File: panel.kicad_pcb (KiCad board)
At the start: 2 copper layers, 25.4 x 52.3 mm, 64 parts, among them U1 DF52-4S-0.8H(21), U2 DF52-4S-0.8H(21), U3 DF52-4S-0.8H(21)

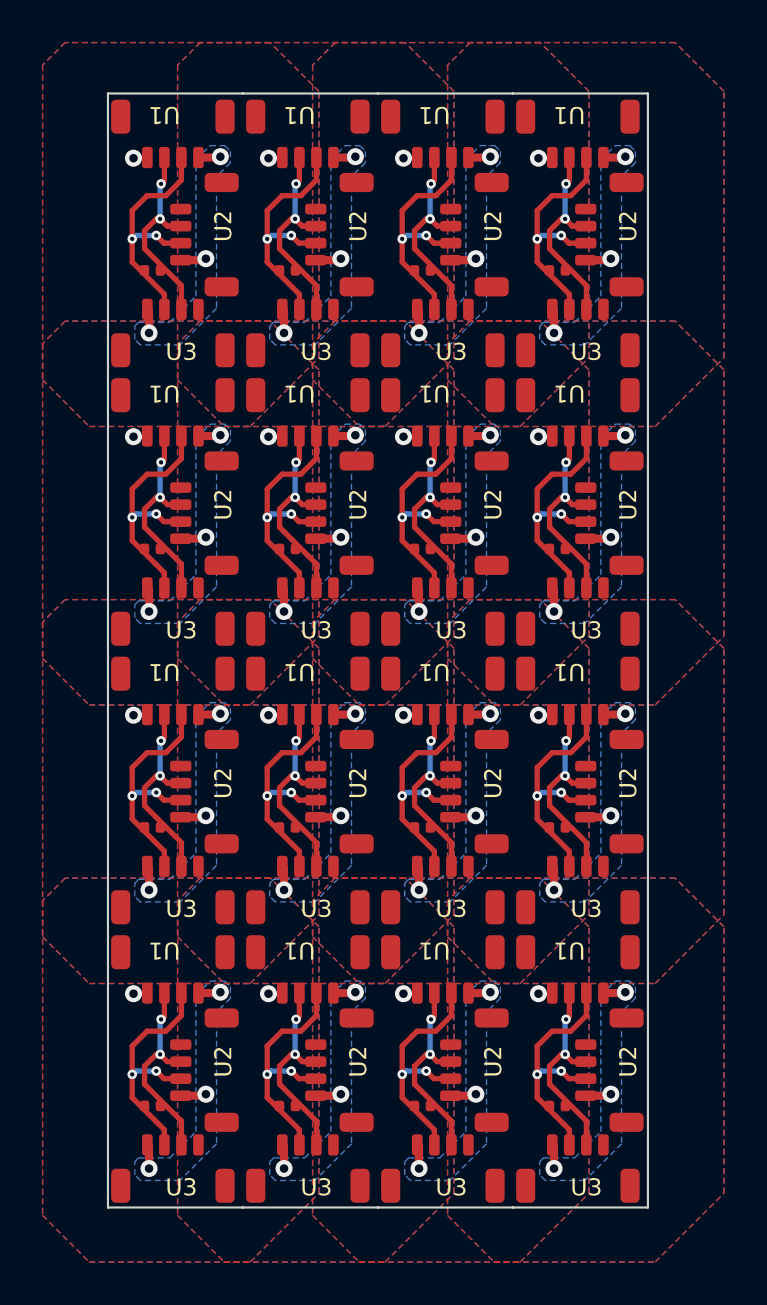
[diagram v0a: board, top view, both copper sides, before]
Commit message: updated gnd for panel. updated panel. updated panel script for better more better
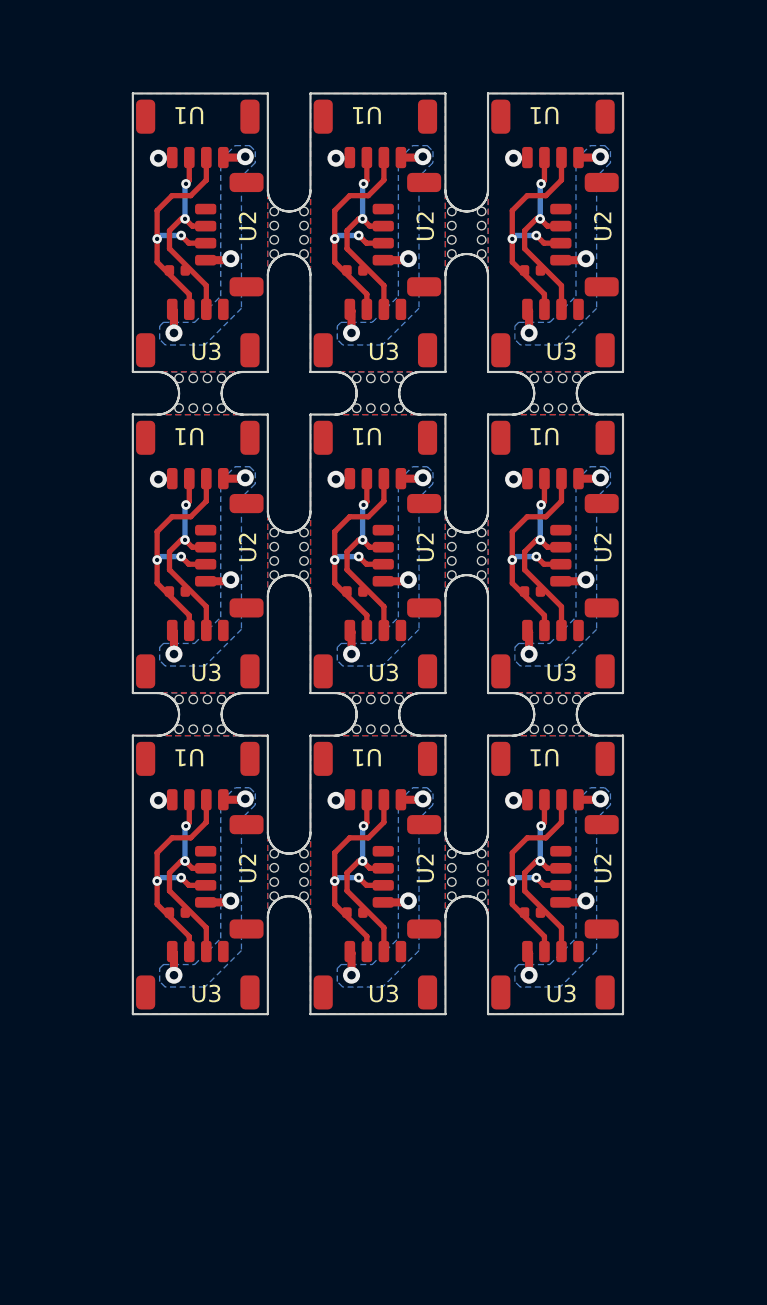
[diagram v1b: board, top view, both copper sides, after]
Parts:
- removed the R1 at (156.9, 67.5)
- removed the R1 at (150.6, 28.3)
- removed the R1 at (137.9, 28.3)
- removed the R1 at (156.9, 41.4)
- removed the R1 at (137.9, 41.4)
- removed the R1 at (137.9, 54.5)
- removed the R1 at (156.9, 28.3)
- removed the R1 at (144.2, 54.5)
- removed the R1 at (150.6, 41.4)
- removed the R1 at (156.9, 54.5)
- removed the R1 at (150.6, 54.5)
- removed the R1 at (144.2, 41.4)
- removed the R1 at (150.6, 67.5)
- removed the R1 at (144.2, 67.5)
- removed the R1 at (137.9, 67.5)
- removed the R1 at (144.2, 28.3)
- removed the U1 at (145.2, 62.2)
- removed the U1 at (157.9, 36.1)
- removed the U1 at (145.2, 49.2)
- removed the U1 at (145.2, 23.0)
- removed the U1 at (138.9, 49.2)
- removed the U1 at (151.6, 62.2)
- removed the U1 at (151.6, 49.2)
- removed the U1 at (157.9, 62.2)
- removed the U1 at (157.9, 23.0)
- removed the U1 at (138.9, 23.0)
- removed the U1 at (151.6, 23.0)
- removed the U1 at (138.9, 36.1)
- removed the U1 at (138.9, 62.2)
- removed the U1 at (157.9, 49.2)
- removed the U1 at (151.6, 36.1)
- removed the U1 at (145.2, 36.1)
- removed the U2 at (158.3, 52.8)
- removed the U2 at (145.6, 65.9)
- removed the U2 at (139.2, 26.6)
- removed the U2 at (145.6, 39.7)
- removed the U2 at (151.9, 39.7)
- removed the U2 at (139.2, 65.9)
- removed the U2 at (151.9, 52.8)
- removed the U2 at (158.3, 65.9)
- removed the U2 at (139.2, 39.7)
- removed the U2 at (151.9, 26.6)
- removed the U2 at (145.6, 26.6)
- removed the U2 at (158.3, 39.7)
- removed the U2 at (145.6, 52.8)
- removed the U2 at (139.2, 52.8)
- removed the U2 at (151.9, 65.9)
- removed the U2 at (158.3, 26.6)
- removed the U3 at (151.6, 56.3)
- removed the U3 at (157.9, 43.2)
- removed the U3 at (145.2, 69.4)
- removed the U3 at (151.6, 43.2)
- removed the U3 at (151.6, 30.1)
- removed the U3 at (145.2, 56.3)
- removed the U3 at (138.9, 56.3)
- removed the U3 at (138.9, 43.2)
- removed the U3 at (138.9, 30.1)
- removed the U3 at (157.9, 69.4)
- removed the U3 at (157.9, 30.1)
- removed the U3 at (138.9, 69.4)
- removed the U3 at (145.2, 30.1)
- removed the U3 at (151.6, 69.4)
- removed the U3 at (157.9, 56.3)
- removed the U3 at (145.2, 43.2)
- added KiKit_MB_10_1: NPTH, NPTH, F.Cu at (141.2, 48.5)
- added KiKit_MB_10_2: NPTH, NPTH, F.Cu at (140.5, 48.5)
- added KiKit_MB_10_3: NPTH, NPTH, F.Cu at (139.8, 48.5)
- added KiKit_MB_10_4: NPTH, NPTH, F.Cu at (139.2, 48.5)
- added KiKit_MB_11_1: NPTH, NPTH, F.Cu at (145.0, 42.6)
- added KiKit_MB_11_2: NPTH, NPTH, F.Cu at (145.0, 42.0)
- added KiKit_MB_11_3: NPTH, NPTH, F.Cu at (145.0, 41.3)
- added KiKit_MB_11_4: NPTH, NPTH, F.Cu at (145.0, 40.6)
- added KiKit_MB_12_1: NPTH, NPTH, F.Cu at (152.0, 40.6)
- added KiKit_MB_12_2: NPTH, NPTH, F.Cu at (152.0, 41.3)
- added KiKit_MB_12_3: NPTH, NPTH, F.Cu at (152.0, 42.0)
- added KiKit_MB_12_4: NPTH, NPTH, F.Cu at (152.0, 42.6)
- added KiKit_MB_13_1: NPTH, NPTH, F.Cu at (147.5, 34.8)
- added KiKit_MB_13_2: NPTH, NPTH, F.Cu at (148.2, 34.8)
- added KiKit_MB_13_3: NPTH, NPTH, F.Cu at (148.8, 34.8)
- added KiKit_MB_13_4: NPTH, NPTH, F.Cu at (149.5, 34.8)
- added KiKit_MB_14_1: NPTH, NPTH, F.Cu at (149.5, 48.5)
- added KiKit_MB_14_2: NPTH, NPTH, F.Cu at (148.8, 48.5)
- added KiKit_MB_14_3: NPTH, NPTH, F.Cu at (148.2, 48.5)
- added KiKit_MB_14_4: NPTH, NPTH, F.Cu at (147.5, 48.5)
- added KiKit_MB_15_1: NPTH, NPTH, F.Cu at (153.4, 42.6)
- added KiKit_MB_15_2: NPTH, NPTH, F.Cu at (153.4, 42.0)
- added KiKit_MB_15_3: NPTH, NPTH, F.Cu at (153.4, 41.3)
- added KiKit_MB_15_4: NPTH, NPTH, F.Cu at (153.4, 40.6)
- added KiKit_MB_16_1: NPTH, NPTH, F.Cu at (155.8, 34.8)
- added KiKit_MB_16_2: NPTH, NPTH, F.Cu at (156.5, 34.8)
- added KiKit_MB_16_3: NPTH, NPTH, F.Cu at (157.2, 34.8)
- added KiKit_MB_16_4: NPTH, NPTH, F.Cu at (157.8, 34.8)
- added KiKit_MB_17_1: NPTH, NPTH, F.Cu at (157.8, 48.5)
- added KiKit_MB_17_2: NPTH, NPTH, F.Cu at (157.2, 48.5)
- added KiKit_MB_17_3: NPTH, NPTH, F.Cu at (156.5, 48.5)
- added KiKit_MB_17_4: NPTH, NPTH, F.Cu at (155.8, 48.5)
- added KiKit_MB_18_1: NPTH, NPTH, F.Cu at (143.6, 55.7)
- added KiKit_MB_18_2: NPTH, NPTH, F.Cu at (143.6, 56.4)
- added KiKit_MB_18_3: NPTH, NPTH, F.Cu at (143.6, 57.0)
- added KiKit_MB_18_4: NPTH, NPTH, F.Cu at (143.6, 57.7)
- added KiKit_MB_19_1: NPTH, NPTH, F.Cu at (139.2, 49.9)
- added KiKit_MB_19_2: NPTH, NPTH, F.Cu at (139.8, 49.9)
- added KiKit_MB_19_3: NPTH, NPTH, F.Cu at (140.5, 49.9)
- added KiKit_MB_19_4: NPTH, NPTH, F.Cu at (141.2, 49.9)
- added KiKit_MB_1_1: NPTH, NPTH, F.Cu at (143.6, 25.5)
- added KiKit_MB_1_2: NPTH, NPTH, F.Cu at (143.6, 26.2)
- added KiKit_MB_1_3: NPTH, NPTH, F.Cu at (143.6, 26.9)
- added KiKit_MB_1_4: NPTH, NPTH, F.Cu at (143.6, 27.5)
- added KiKit_MB_20_1: NPTH, NPTH, F.Cu at (145.0, 57.7)
- added KiKit_MB_20_2: NPTH, NPTH, F.Cu at (145.0, 57.0)
- added KiKit_MB_20_3: NPTH, NPTH, F.Cu at (145.0, 56.4)
- added KiKit_MB_20_4: NPTH, NPTH, F.Cu at (145.0, 55.7)
- added KiKit_MB_21_1: NPTH, NPTH, F.Cu at (152.0, 55.7)
- added KiKit_MB_21_2: NPTH, NPTH, F.Cu at (152.0, 56.4)
- added KiKit_MB_21_3: NPTH, NPTH, F.Cu at (152.0, 57.0)
- added KiKit_MB_21_4: NPTH, NPTH, F.Cu at (152.0, 57.7)
- added KiKit_MB_22_1: NPTH, NPTH, F.Cu at (147.5, 49.9)
- added KiKit_MB_22_2: NPTH, NPTH, F.Cu at (148.2, 49.9)
- added KiKit_MB_22_3: NPTH, NPTH, F.Cu at (148.8, 49.9)
- added KiKit_MB_22_4: NPTH, NPTH, F.Cu at (149.5, 49.9)
- added KiKit_MB_23_1: NPTH, NPTH, F.Cu at (153.4, 57.7)
- added KiKit_MB_23_2: NPTH, NPTH, F.Cu at (153.4, 57.0)
- added KiKit_MB_23_3: NPTH, NPTH, F.Cu at (153.4, 56.4)
- added KiKit_MB_23_4: NPTH, NPTH, F.Cu at (153.4, 55.7)
- added KiKit_MB_24_1: NPTH, NPTH, F.Cu at (155.8, 49.9)
- added KiKit_MB_24_2: NPTH, NPTH, F.Cu at (156.5, 49.9)
- added KiKit_MB_24_3: NPTH, NPTH, F.Cu at (157.2, 49.9)
- added KiKit_MB_24_4: NPTH, NPTH, F.Cu at (157.8, 49.9)
- added KiKit_MB_2_1: NPTH, NPTH, F.Cu at (141.2, 33.4)
- added KiKit_MB_2_2: NPTH, NPTH, F.Cu at (140.5, 33.4)
- added KiKit_MB_2_3: NPTH, NPTH, F.Cu at (139.8, 33.4)
- added KiKit_MB_2_4: NPTH, NPTH, F.Cu at (139.2, 33.4)
- added KiKit_MB_3_1: NPTH, NPTH, F.Cu at (145.0, 27.5)
- added KiKit_MB_3_2: NPTH, NPTH, F.Cu at (145.0, 26.9)
- added KiKit_MB_3_3: NPTH, NPTH, F.Cu at (145.0, 26.2)
- added KiKit_MB_3_4: NPTH, NPTH, F.Cu at (145.0, 25.5)
- added KiKit_MB_4_1: NPTH, NPTH, F.Cu at (152.0, 25.5)
- added KiKit_MB_4_2: NPTH, NPTH, F.Cu at (152.0, 26.2)
- added KiKit_MB_4_3: NPTH, NPTH, F.Cu at (152.0, 26.9)
- added KiKit_MB_4_4: NPTH, NPTH, F.Cu at (152.0, 27.5)
- added KiKit_MB_5_1: NPTH, NPTH, F.Cu at (149.5, 33.4)
- added KiKit_MB_5_2: NPTH, NPTH, F.Cu at (148.8, 33.4)
- added KiKit_MB_5_3: NPTH, NPTH, F.Cu at (148.2, 33.4)
- added KiKit_MB_5_4: NPTH, NPTH, F.Cu at (147.5, 33.4)
- added KiKit_MB_6_1: NPTH, NPTH, F.Cu at (153.4, 27.5)
- added KiKit_MB_6_2: NPTH, NPTH, F.Cu at (153.4, 26.9)
- added KiKit_MB_6_3: NPTH, NPTH, F.Cu at (153.4, 26.2)
- added KiKit_MB_6_4: NPTH, NPTH, F.Cu at (153.4, 25.5)
- added KiKit_MB_7_1: NPTH, NPTH, F.Cu at (157.8, 33.4)
- added KiKit_MB_7_2: NPTH, NPTH, F.Cu at (157.2, 33.4)
- added KiKit_MB_7_3: NPTH, NPTH, F.Cu at (156.5, 33.4)
- added KiKit_MB_7_4: NPTH, NPTH, F.Cu at (155.8, 33.4)
- added KiKit_MB_8_1: NPTH, NPTH, F.Cu at (143.6, 40.6)
- added KiKit_MB_8_2: NPTH, NPTH, F.Cu at (143.6, 41.3)
- added KiKit_MB_8_3: NPTH, NPTH, F.Cu at (143.6, 42.0)
- added KiKit_MB_8_4: NPTH, NPTH, F.Cu at (143.6, 42.6)
- added KiKit_MB_9_1: NPTH, NPTH, F.Cu at (139.2, 34.8)
- added KiKit_MB_9_2: NPTH, NPTH, F.Cu at (139.8, 34.8)
- added KiKit_MB_9_3: NPTH, NPTH, F.Cu at (140.5, 34.8)
- added KiKit_MB_9_4: NPTH, NPTH, F.Cu at (141.2, 34.8)
- added R1: 120 0402, can-b2b-interconnect:R_0402_1005Metric, F.Cu at (155.8, 28.3)
- added R1: 120 0402, can-b2b-interconnect:R_0402_1005Metric, F.Cu at (155.8, 43.4)
- added R1: 120 0402, can-b2b-interconnect:R_0402_1005Metric, F.Cu at (147.4, 28.3)
- added R1: 120 0402, can-b2b-interconnect:R_0402_1005Metric, F.Cu at (147.4, 58.5)
- added R1: 120 0402, can-b2b-interconnect:R_0402_1005Metric, F.Cu at (147.4, 43.4)
- added R1: 120 0402, can-b2b-interconnect:R_0402_1005Metric, F.Cu at (155.8, 58.5)
- added R1: 120 0402, can-b2b-interconnect:R_0402_1005Metric, F.Cu at (139.1, 28.3)
- added R1: 120 0402, can-b2b-interconnect:R_0402_1005Metric, F.Cu at (139.1, 43.4)
- added R1: 120 0402, can-b2b-interconnect:R_0402_1005Metric, F.Cu at (139.1, 58.5)
- added U1: DF52-4S-0.8H(21), can-b2b-interconnect:DF52-4S-0.8H(21), F.Cu at (148.4, 38.1)
- added U1: DF52-4S-0.8H(21), can-b2b-interconnect:DF52-4S-0.8H(21), F.Cu at (148.4, 53.2)
- added U1: DF52-4S-0.8H(21), can-b2b-interconnect:DF52-4S-0.8H(21), F.Cu at (148.4, 23.0)
- added U1: DF52-4S-0.8H(21), can-b2b-interconnect:DF52-4S-0.8H(21), F.Cu at (140.0, 38.1)
- added U1: DF52-4S-0.8H(21), can-b2b-interconnect:DF52-4S-0.8H(21), F.Cu at (156.7, 23.0)
- added U1: DF52-4S-0.8H(21), can-b2b-interconnect:DF52-4S-0.8H(21), F.Cu at (156.7, 38.1)
- added U1: DF52-4S-0.8H(21), can-b2b-interconnect:DF52-4S-0.8H(21), F.Cu at (140.0, 23.0)
- added U1: DF52-4S-0.8H(21), can-b2b-interconnect:DF52-4S-0.8H(21), F.Cu at (140.0, 53.2)
- added U1: DF52-4S-0.8H(21), can-b2b-interconnect:DF52-4S-0.8H(21), F.Cu at (156.7, 53.2)
- added U2: DF52-4S-0.8H(21), can-b2b-interconnect:DF52-4S-0.8H(21), F.Cu at (148.8, 41.7)
- added U2: DF52-4S-0.8H(21), can-b2b-interconnect:DF52-4S-0.8H(21), F.Cu at (157.1, 41.7)
- added U2: DF52-4S-0.8H(21), can-b2b-interconnect:DF52-4S-0.8H(21), F.Cu at (140.4, 26.6)
- added U2: DF52-4S-0.8H(21), can-b2b-interconnect:DF52-4S-0.8H(21), F.Cu at (157.1, 26.6)
- added U2: DF52-4S-0.8H(21), can-b2b-interconnect:DF52-4S-0.8H(21), F.Cu at (148.8, 56.8)
- added U2: DF52-4S-0.8H(21), can-b2b-interconnect:DF52-4S-0.8H(21), F.Cu at (140.4, 41.7)
- added U2: DF52-4S-0.8H(21), can-b2b-interconnect:DF52-4S-0.8H(21), F.Cu at (140.4, 56.8)
- added U2: DF52-4S-0.8H(21), can-b2b-interconnect:DF52-4S-0.8H(21), F.Cu at (157.1, 56.8)
- added U2: DF52-4S-0.8H(21), can-b2b-interconnect:DF52-4S-0.8H(21), F.Cu at (148.8, 26.6)
- added U3: DF52-4S-0.8H(21), can-b2b-interconnect:DF52-4S-0.8H(21), F.Cu at (156.7, 60.3)
- added U3: DF52-4S-0.8H(21), can-b2b-interconnect:DF52-4S-0.8H(21), F.Cu at (156.7, 30.1)
- added U3: DF52-4S-0.8H(21), can-b2b-interconnect:DF52-4S-0.8H(21), F.Cu at (140.0, 30.1)
- added U3: DF52-4S-0.8H(21), can-b2b-interconnect:DF52-4S-0.8H(21), F.Cu at (148.4, 30.1)
- added U3: DF52-4S-0.8H(21), can-b2b-interconnect:DF52-4S-0.8H(21), F.Cu at (156.7, 45.2)
- added U3: DF52-4S-0.8H(21), can-b2b-interconnect:DF52-4S-0.8H(21), F.Cu at (140.0, 45.2)
- added U3: DF52-4S-0.8H(21), can-b2b-interconnect:DF52-4S-0.8H(21), F.Cu at (148.4, 60.3)
- added U3: DF52-4S-0.8H(21), can-b2b-interconnect:DF52-4S-0.8H(21), F.Cu at (148.4, 45.2)
- added U3: DF52-4S-0.8H(21), can-b2b-interconnect:DF52-4S-0.8H(21), F.Cu at (140.0, 60.3)
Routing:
- net Board_11-/CANL: track 11.7 -> 0.00 mm, vias 2 -> 0
- net Board_15-/CANL: track 11.7 -> 0.00 mm, vias 2 -> 0
- net Board_10-/CANL: track 11.7 -> 0.00 mm, vias 2 -> 0
- net Board_14-/CANL: track 11.7 -> 0.00 mm, vias 2 -> 0
- net Board_9-/CANL: track 11.7 -> 0.00 mm, vias 2 -> 0
- net Board_12-/CANL: track 11.7 -> 0.00 mm, vias 2 -> 0
- net Board_13-/CANL: track 11.7 -> 0.00 mm, vias 2 -> 0
- net Board_9-/CANH: track 9.45 -> 0.00 mm, vias 2 -> 0
- net Board_13-/CANH: track 9.45 -> 0.00 mm, vias 2 -> 0
- net Board_12-/CANH: track 9.45 -> 0.00 mm, vias 2 -> 0
- net Board_11-/CANH: track 9.45 -> 0.00 mm, vias 2 -> 0
- net Board_10-/CANH: track 9.45 -> 0.00 mm, vias 2 -> 0
- net Board_15-/CANH: track 9.45 -> 0.00 mm, vias 2 -> 0
- net Board_14-/CANH: track 9.45 -> 0.00 mm, vias 2 -> 0
- net Board_10-/VBAT: track 3.40 -> 0.00 mm, vias 3 -> 0
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- removed copper zone on B.Cu, net Board_10-/VBAT
- removed copper zone on B.Cu, net Board_10-GND
- removed copper zone on F.Cu, net Board_10-GND
- removed copper zone on B.Cu, net Board_11-/VBAT
- removed copper zone on B.Cu, net Board_11-GND
- removed copper zone on F.Cu, net Board_11-GND
- removed copper zone on B.Cu, net Board_12-/VBAT
- removed copper zone on B.Cu, net Board_12-GND
- removed copper zone on F.Cu, net Board_12-GND
- removed copper zone on B.Cu, net Board_13-/VBAT
- removed copper zone on B.Cu, net Board_13-GND
- removed copper zone on F.Cu, net Board_13-GND
- removed copper zone on B.Cu, net Board_14-/VBAT
- removed copper zone on B.Cu, net Board_14-GND
- removed copper zone on F.Cu, net Board_14-GND
- removed copper zone on B.Cu, net Board_15-/VBAT
- removed copper zone on B.Cu, net Board_15-GND
- removed copper zone on F.Cu, net Board_15-GND
- removed copper zone on B.Cu, net Board_9-/VBAT
- removed copper zone on B.Cu, net Board_9-GND
- removed copper zone on F.Cu, net Board_9-GND
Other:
- board size 25.4 x 52.3 mm -> 23 x 43.2 mm
- board text removed: "V-CUT"
